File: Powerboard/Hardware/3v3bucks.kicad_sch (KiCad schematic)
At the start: 26 parts, among them IC2 SiC437AED-T1-GE3, Q5 PXP012-30QLJ, Q6 PXP012-30QLJ, U1 LTC4412xS6, U8 LTC4412xS6

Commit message: shiven layout change
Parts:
- C40: value 47uF -> 100uF; footprint Capacitor_SMD:C_1206_3216Metric -> iclr:CAPPM7362X200N
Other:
- note added: "TCN4107M035R0100E"
- note removed: "Sim says up to 330uF on input for 12V, formulas suggest 20uF should suffice. N.B. formula uses Vcinpkpk of 500mV (upper bound)"

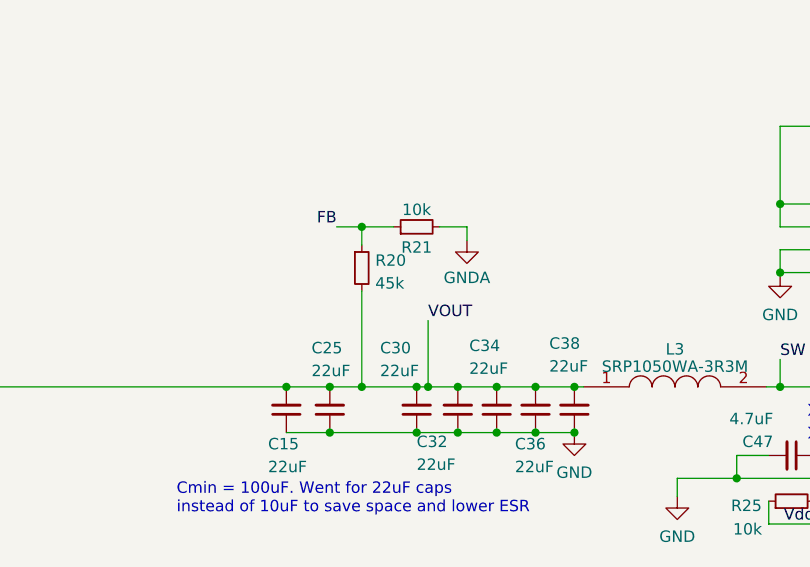
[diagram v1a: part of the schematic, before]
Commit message: fixed resistor value
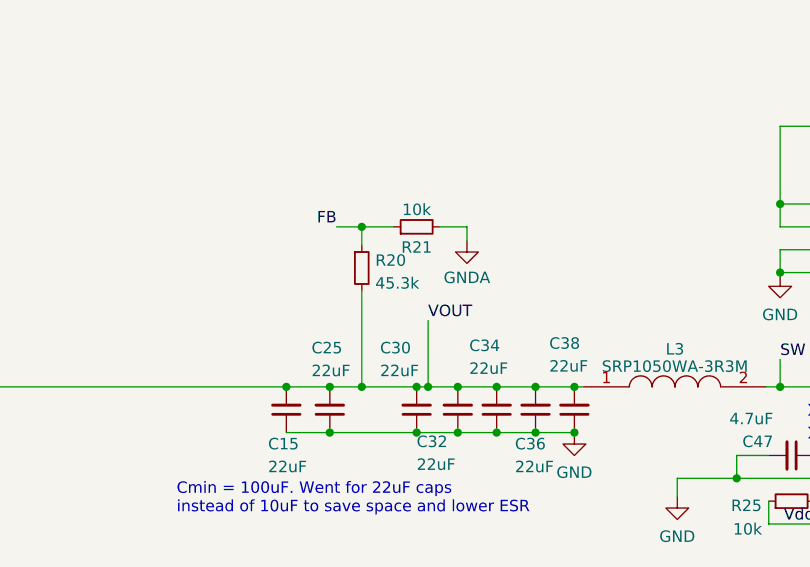
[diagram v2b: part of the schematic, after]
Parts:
- C15, C25, C30, C32, C34, C36, C38: MPN (none) -> CGA0603X5R226M160JT
- IC2: MPN (none) -> SIC437AED-T1-GE3
- R20: value 45k -> 45.3k
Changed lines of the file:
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@@
+			)
+		)
+		(property "MPN" " CGA0603X5R226M160JT"
+			(at 71.12 114.808 0)
+			(effects
+				(font
+					(size 1.27 1.27)
+				)
+				(hide yes)
 			)
 		)
@@
 			)
 		)
-		(property "Value" "45k"
+		(property "Value" "45.3k"
 			(at 66.5226 100.7622 0)
 			(effects
@@
 			)
 		)
+		(property "MPN" " SIC437AED-T1-GE3"
+			(at 115.316 91.948 0)
+			(effects
+				(font
+					(size 1.27 1.27)
+				)
+				(hide yes)
+			)
+		)
 		(pin "1"
 		)
@@
 		)
 		(property "Description" ""
+			(at 75.692 114.808 0)
+			(effects
+				(font
+					(size 1.27 1.27)
+				)
+				(hide yes)
+			)
+		)
+		(property "MPN" " CGA0603X5R226M160JT"
 			(at 75.692 114.808 0)
 			(effects
@@
 			)
 		)
+		(property "MPN" " CGA0603X5R226M160JT"
+			(at 61.468 114.808 0)
+			(effects
+				(font
+					(size 1.27 1.27)
+				)
+				(hide yes)
+			)
+		)
 		(pin "1"
 		)
@@
 			)
 		)
+		(property "MPN" " CGA0603X5R226M160JT"
+			(at 88.646 114.808 0)
+			(effects
+				(font
+					(size 1.27 1.27)
+				)
+				(hide yes)
+			)
+		)
 		(pin "1"
 		)
@@
 			)
 		)
+		(property "MPN" " CGA0603X5R226M160JT"
+			(at 56.642 114.808 0)
+			(effects
+				(font
+					(size 1.27 1.27)
+				)
+				(hide yes)
+			)
+		)
 		(pin "1"
 		)
@@
 			)
 		)
+		(property "MPN" " CGA0603X5R226M160JT"
+			(at 80.01 114.808 0)
+			(effects
+				(font
+					(size 1.27 1.27)
+				)
+				(hide yes)
+			)
+		)
 		(pin "1"
 		)
@@
 			(at 84.328 114.808 0)
 			(effects
+				(font
+					(size 1.27 1.27)
+				)
+				(hide yes)
+			)
+		)
+		(property "MPN" " CGA0603X5R226M160JT"
+			(at 84.328 114.808 0)
+			(effects

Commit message: updated mpn on some caps
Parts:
- C44: MPN (none) -> C1005X7R1H104KT000S
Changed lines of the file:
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@@
+			)
+		)
+		(property "MPN" " C1005X7R1H104KT000S"
+			(at 181.864 85.852 0)
+			(effects
+				(font
+					(size 1.27 1.27)
+				)
+				(hide yes)
 			)
 		)

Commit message: post Andrei review
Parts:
- added C12: 2.2uF, Capacitor_SMD:C_0402_1005Metric, symbol Device:C_Small
- added R47: 100k, Resistor_SMD:R_0402_1005Metric, symbol Device:R_Small
- C16: value 680pF -> TBD
- R37: value 5.1 -> TBD
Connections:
- net GND: now also R47.2
- net VBUS: now also C12.1
- net at Q6.4 (G), U8.5 (GATE): now also C12.2, R47.1
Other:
- moved on the sheet: U8
